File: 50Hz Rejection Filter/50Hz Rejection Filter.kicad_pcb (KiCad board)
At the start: 2 copper layers, 39.4 x 20.8 mm, 10 parts, among them U1 TL072

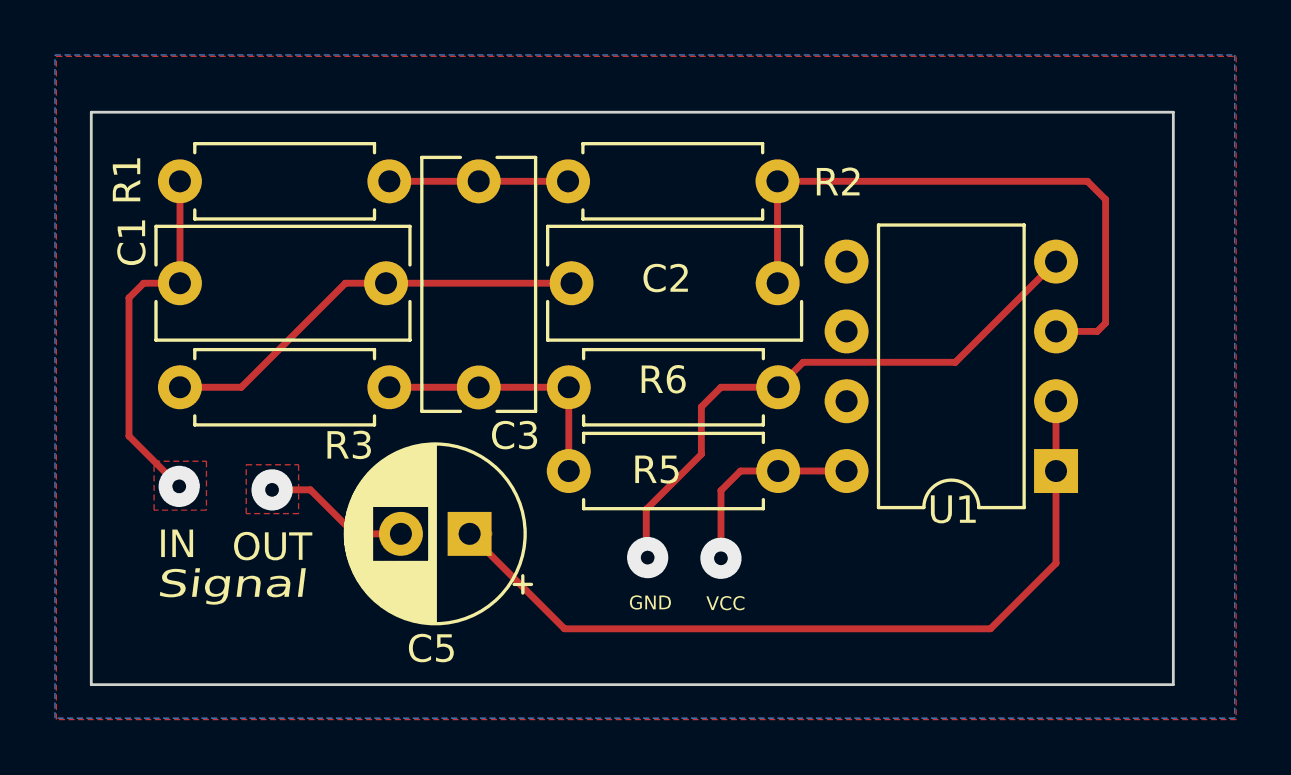
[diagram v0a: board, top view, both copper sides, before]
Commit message: Signal GND Pad added
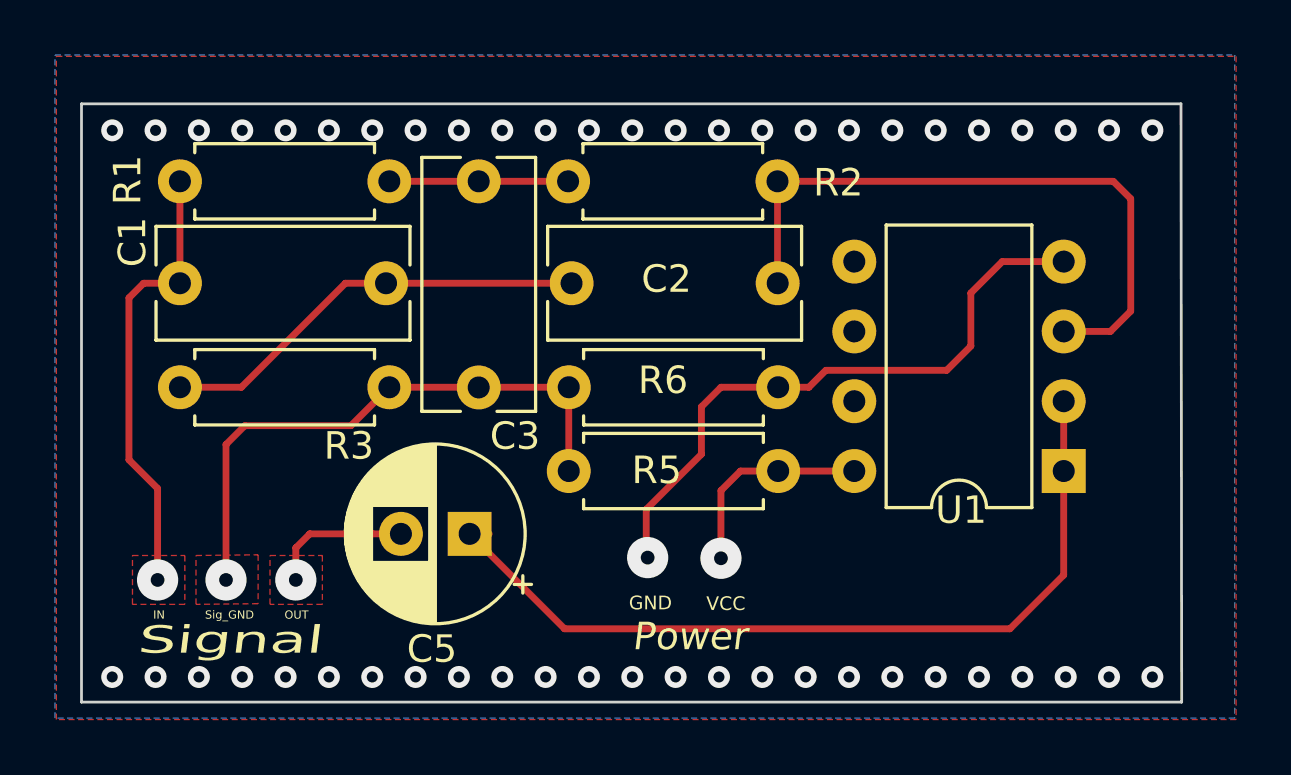
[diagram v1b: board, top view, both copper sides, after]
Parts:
- moved U1 0.28 mm to (156.0, 106.5)
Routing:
- net GNDREF: track 9.58 -> 21.3 mm, vias 0 -> 51
- net Signal_IN: track 13.4 -> 16.7 mm
- net GND: track 21.4 -> 22.8 mm
- net Net-(C2-Pad2): track 22.3 -> 23.7 mm
- net Net-(C5-Pad1): track 30.4 -> 30.9 mm
- net Signal_OUT: track 5.35 -> 5.86 mm
- added copper zone on B.Cu, net GNDREF
- added copper zone on F.Cu, net GNDREF
- removed copper zone on B.Cu, net GND
- removed copper zone on F.Cu, net GND
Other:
- board size 39.4 x 20.8 mm -> 40 x 21.8 mm
- board text added: "Power"
- board text added: "Sig_GND"
